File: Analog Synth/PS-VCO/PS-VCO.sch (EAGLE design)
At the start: 44 parts, among them IC1 TL084D, Q1 BC847BS, Q2 2N3906, T1 2N3904, T2 2N3904

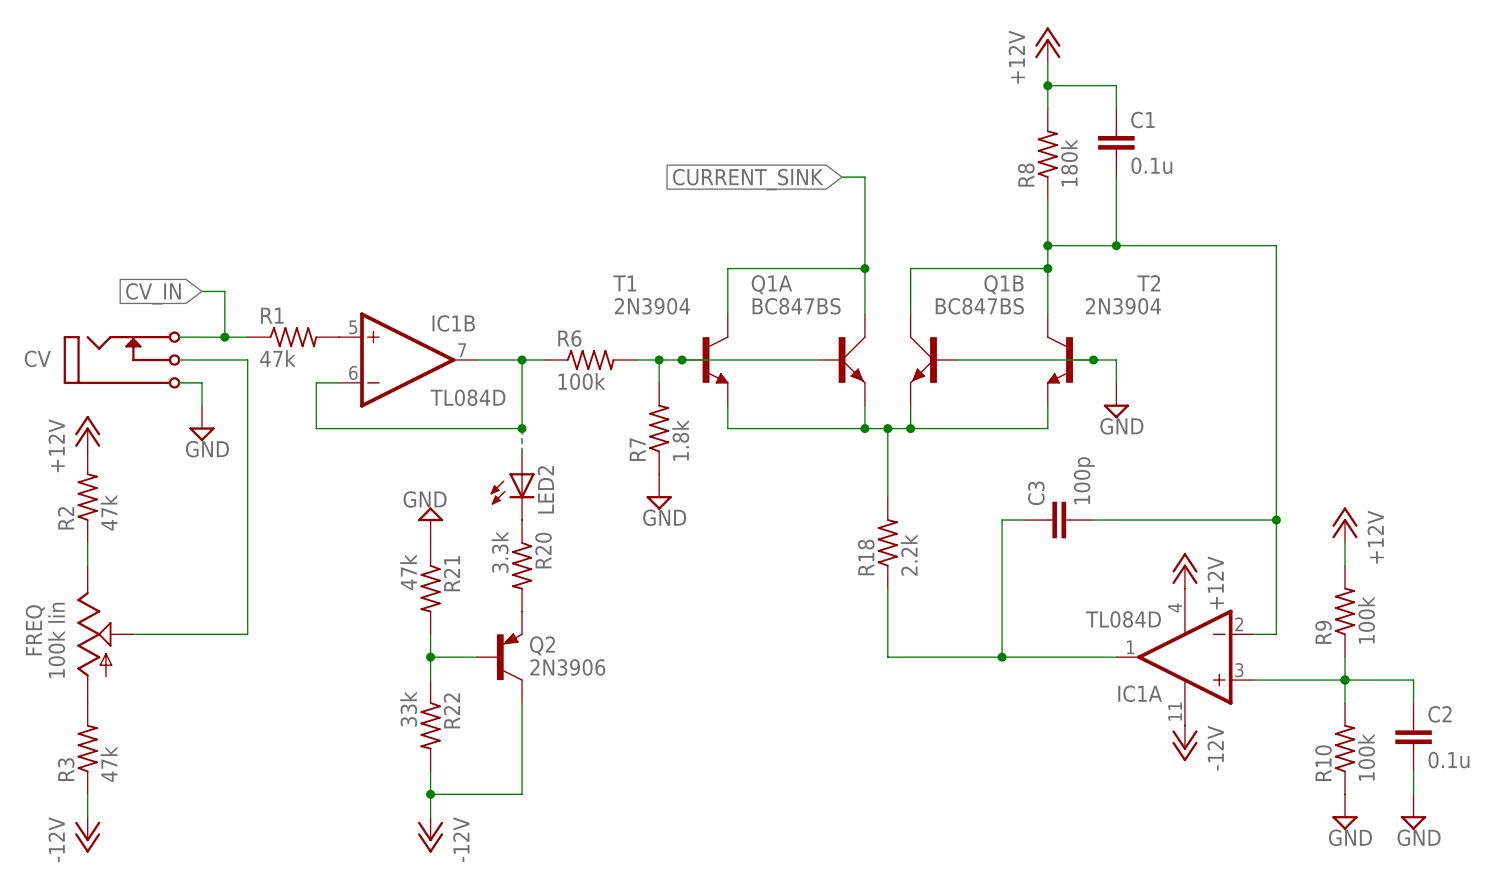
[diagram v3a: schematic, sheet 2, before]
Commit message: PS-VCO: updating documentation and schematic. rendered pdfs for schematic and pcb. generated a BOM
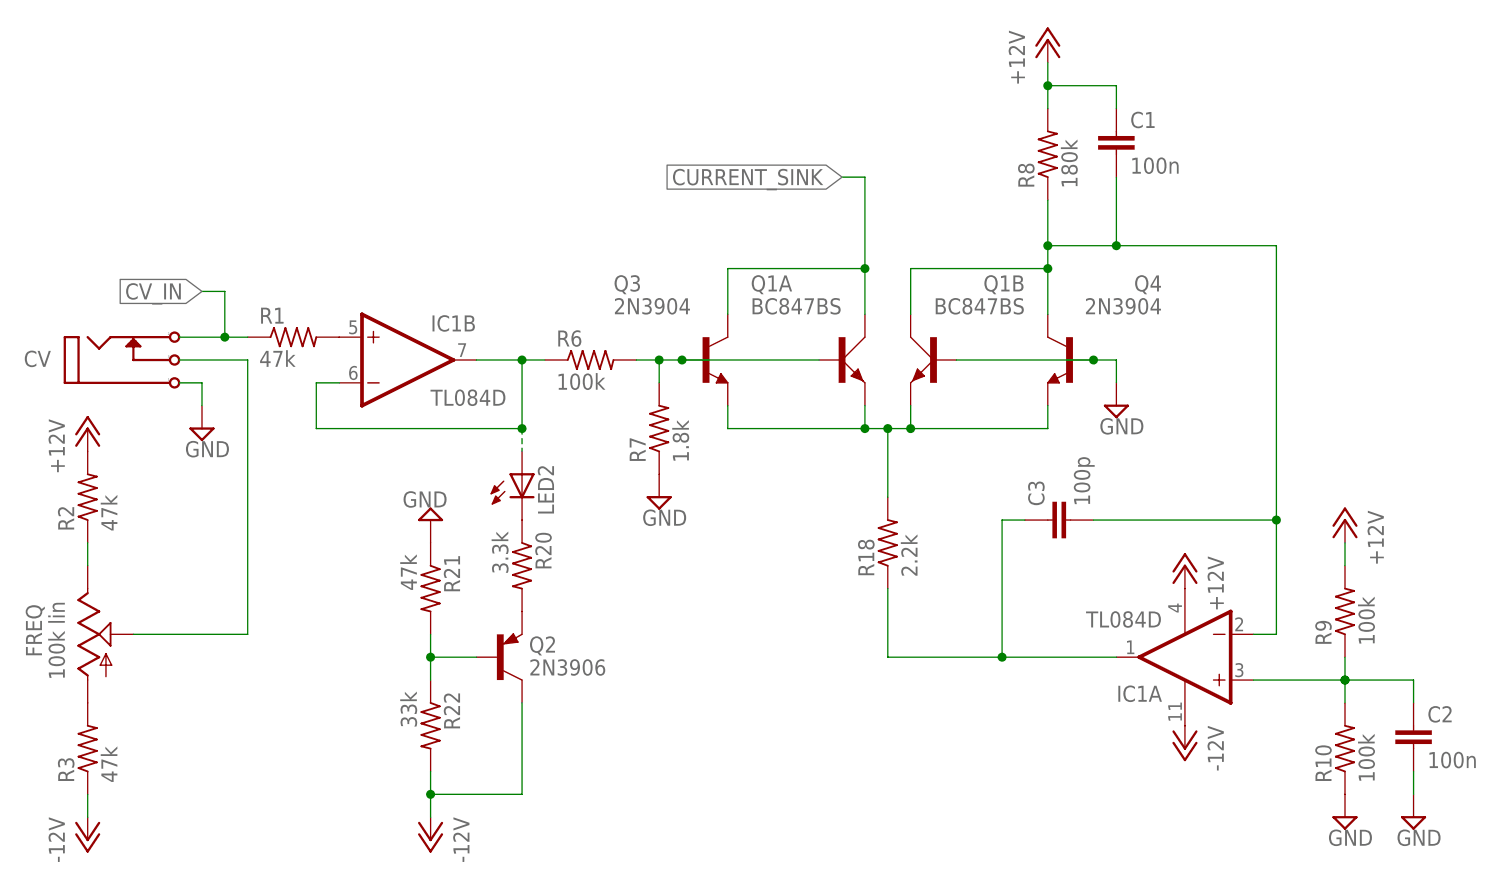
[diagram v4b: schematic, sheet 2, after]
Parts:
- C1, C2, C5: value 0.1u -> 100n
- CV: value I/O -> CV
- renumbered T1 to Q3, T2 to Q4, U$2 to Q5
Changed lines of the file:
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@@
 <parts>
 <part name="IC1" library="linear" deviceset="TL084" device="D"/>
-<part name="CV" library="!synth_sch" deviceset="MONO_JACK" device="" value="I/O"/>
+<part name="CV" library="!synth_sch" deviceset="MONO_JACK" device="" value="CV"/>
 <part name="Q1" library="transistor-small-signal" deviceset="BC847BS" device=""/>
-<part name="T1" library="transistor" deviceset="2N3904" device=""/>
-<part name="T2" library="transistor" deviceset="2N3904" device=""/>
+<part name="Q3" library="transistor" deviceset="2N3904" device=""/>
+<part name="Q4" library="transistor" deviceset="2N3904" device=""/>
 <part name="R1" library="rcl" deviceset="R-US_" device="R0603" value="47k"/>
 <part name="FREQ" library="pot" deviceset="TRIM_US-" device="B64Y" value="100k lin"/>
@@
 <part name="R7" library="rcl" deviceset="R-US_" device="R0603" value="1.8k"/>
 <part name="SUPPLY4" library="supply2" deviceset="GND" device=""/>
-<part name="C1" library="rcl" deviceset="C-EU" device="C0603" value="0.1u"/>
+<part name="C1" library="rcl" deviceset="C-EU" device="C0603" value="100n"/>
 <part name="R8" library="rcl" deviceset="R-US_" device="R0603" value="180k"/>
-<part name="C2" library="rcl" deviceset="C-EU" device="C0603" value="0.1u"/>
+<part name="C2" library="rcl" deviceset="C-EU" device="C0603" value="100n"/>
 <part name="R9" library="rcl" deviceset="R-US_" device="R0603" value="100k"/>
 <part name="R10" library="rcl" deviceset="R-US_" device="R0603" value="100k"/>
@@
 <part name="R12" library="rcl" deviceset="R-US_" device="R0603" value="4.7"/>
 <part name="JP2" library="pinhead" deviceset="PINHD-2X5" device=""/>
-<part name="U$2" library="!synth_sch" deviceset="2N7000" device=""/>
+<part name="Q5" library="!synth_sch" deviceset="2N7000" device=""/>
 <part name="SQUARE" library="!synth_sch" deviceset="MONO_JACK" device="" value="I/O"/>
 <part name="R4" library="rcl" deviceset="R-US_" device="R0603" value="27k"/>
-<part name="C5" library="rcl" deviceset="C-EU" device="C0603" value="0.1u"/>
+<part name="C5" library="rcl" deviceset="C-EU" device="C0603" value="100n"/>
 <part name="R5" library="rcl" deviceset="R-US_" device="R0603" value="100k"/>
 <part name="R13" library="rcl" deviceset="R-US_" device="R0603" value="100k"/>
@@
 <attribute name="VALUE" x="116.84" y="91.44" size="1.778" layer="96" rot="MR0"/>
 </instance>
-<instance part="T1" gate="G1" x="81.28" y="86.36"/>
-<instance part="T2" gate="G1" x="121.92" y="86.36" rot="MR0"/>
+<instance part="Q3" gate="G1" x="81.28" y="86.36"/>
+<instance part="Q4" gate="G1" x="121.92" y="86.36" rot="MR0"/>
 <instance part="R1" gate="G$1" x="35.56" y="88.9"/>
 <instance part="FREQ" gate="G$1" x="12.7" y="55.88" smashed="yes">
@@
 <pinref part="Q1" gate="A" pin="C"/>
 <wire x1="99.06" y1="91.44" x2="99.06" y2="96.52" width="0.1524" layer="91"/>
-<pinref part="T1" gate="G1" pin="C"/>
+<pinref part="Q3" gate="G1" pin="C"/>
 <wire x1="99.06" y1="96.52" x2="83.82" y2="96.52" width="0.1524" layer="91"/>
 <wire x1="83.82" y1="96.52" x2="83.82" y2="91.44" width="0.1524" layer="91"/>
@@
 <wire x1="99.06" y1="81.28" x2="99.06" y2="78.74" width="0.1524" layer="91"/>
 <wire x1="99.06" y1="78.74" x2="83.82" y2="78.74" width="0.1524" layer="91"/>
-<pinref part="T1" gate="G1" pin="E"/>
+<pinref part="Q3" gate="G1" pin="E"/>
 <wire x1="83.82" y1="78.74" x2="83.82" y2="81.28" width="0.1524" layer="91"/>
 <pinref part="Q1" gate="B" pin="E"/>
 <wire x1="104.14" y1="81.28" x2="104.14" y2="78.74" width="0.1524" layer="91"/>
 <wire x1="104.14" y1="78.74" x2="119.38" y2="78.74" width="0.1524" layer="91"/>
-<pinref part="T2" gate="G1" pin="E"/>
+<pinref part="Q4" gate="G1" pin="E"/>
 <wire x1="119.38" y1="78.74" x2="119.38" y2="81.28" width="0.1524" layer="91"/>
 <junction x="104.14" y="78.74"/>
@@
 <pinref part="Q1" gate="A" pin="B"/>
 <wire x1="93.98" y1="86.36" x2="78.74" y2="86.36" width="0.1524" layer="91"/>
-<pinref part="T1" gate="G1" pin="B"/>
+<pinref part="Q3" gate="G1" pin="B"/>
 <wire x1="76.2" y1="86.36" x2="78.74" y2="86.36" width="0.1524" layer="91"/>
 <junction x="78.74" y="86.36"/>
@@
 <pinref part="Q1" gate="B" pin="B"/>
 <wire x1="109.22" y1="86.36" x2="124.46" y2="86.36" width="0.1524" layer="91"/>
-<pinref part="T2" gate="G1" pin="B"/>
+<pinref part="Q4" gate="G1" pin="B"/>
 <wire x1="127" y1="86.36" x2="124.46" y2="86.36" width="0.1524" layer="91"/>
 <junction x="124.46" y="86.36"/>
@@
 <pinref part="Q1" gate="B" pin="C"/>
 <wire x1="104.14" y1="91.44" x2="104.14" y2="96.52" width="0.1524" layer="91"/>
-<pinref part="T2" gate="G1" pin="C"/>
+<pinref part="Q4" gate="G1" pin="C"/>
 <wire x1="104.14" y1="96.52" x2="119.38" y2="96.52" width="0.1524" layer="91"/>
 <wire x1="119.38" y1="96.52" x2="119.38" y2="91.44" width="0.1524" layer="91"/>
@@
 <instance part="IC1" gate="C" x="50.8" y="58.42"/>
 <instance part="IC1" gate="D" x="33.02" y="5.08"/>
-<instance part="U$2" gate="G$1" x="30.48" y="88.9" rot="MR0"/>
+<instance part="Q5" gate="G$1" x="30.48" y="88.9" rot="MR0"/>
 <instance part="SQUARE" gate="J1" x="88.9" y="2.54" rot="MR0"/>
 <instance part="R4" gate="G$1" x="40.64" y="76.2" rot="R90"/>
@@
 </segment>
 <segment>
-<pinref part="U$2" gate="G$1" pin="D"/>
+<pinref part="Q5" gate="G$1" pin="D"/>
 <pinref part="P+1" gate="1" pin="+12V"/>
 <wire x1="25.4" y1="91.44" x2="25.4" y2="96.52" width="0.1524" layer="91"/>
@@
 <wire x1="27.94" y1="53.34" x2="27.94" y2="55.88" width="0.1524" layer="91"/>
 <junction x="27.94" y="55.88"/>
-<pinref part="U$2" gate="G$1" pin="S"/>
+<pinref part="Q5" gate="G$1" pin="S"/>
 <wire x1="25.4" y1="86.36" x2="25.4" y2="55.88" width="0.1524" layer="91"/>
 <junction x="25.4" y="55.88"/>
@@
 <wire x1="60.96" y1="68.58" x2="60.96" y2="88.9" width="0.1524" layer="91"/>
 <wire x1="60.96" y1="88.9" x2="33.02" y2="88.9" width="0.1524" layer="91"/>
-<pinref part="U$2" gate="G$1" pin="G"/>
+<pinref part="Q5" gate="G$1" pin="G"/>
 <junction x="60.96" y="68.58"/>
 </segment>

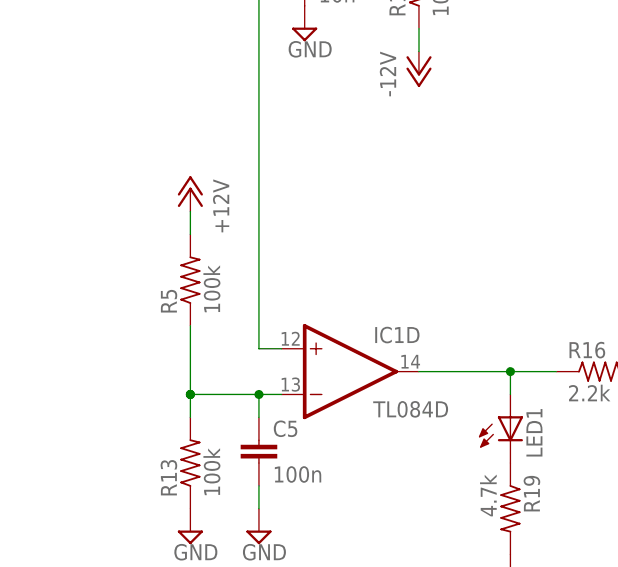
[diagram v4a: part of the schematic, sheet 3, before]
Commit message: updating PS-VCO. Changed a resistor value to get closer to 50% duty cycle. It is still very approximate, but before the duty cycle was around 25% or 30% or something really obviously not balanced.
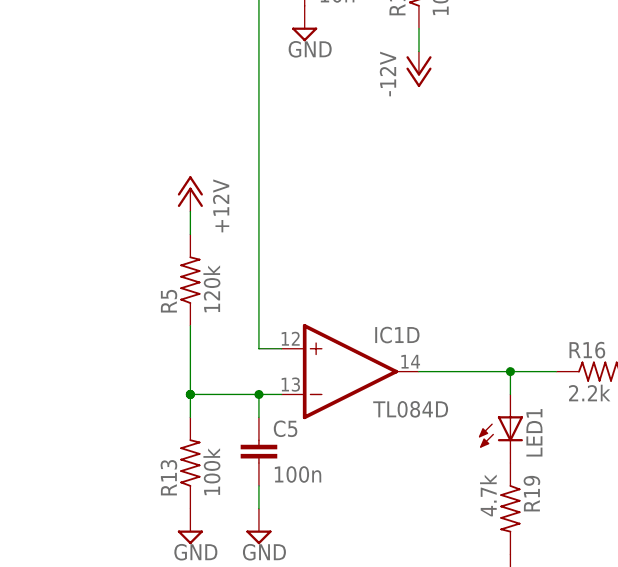
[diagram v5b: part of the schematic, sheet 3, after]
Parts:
- R5: value 100k -> 120k
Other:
- note added: "An attempt at creating a minimalistic VCO."
- note added: "This op amp (configured as a comparator) is set up to output a square wave at approximately 50% duty cycle. The amplitude of the output square wave should be just slightly less than 50% of the power rail voltage."
- note removed: "An attempt at creasing minimalistic VCO."
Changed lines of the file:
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@@
 <part name="R4" library="rcl" deviceset="R-US_" device="R0603" value="27k"/>
 <part name="C5" library="rcl" deviceset="C-EU" device="C0603" value="100n"/>
-<part name="R5" library="rcl" deviceset="R-US_" device="R0603" value="100k"/>
+<part name="R5" library="rcl" deviceset="R-US_" device="R0603" value="120k"/>
 <part name="R13" library="rcl" deviceset="R-US_" device="R0603" value="100k"/>
 <part name="C6" library="rcl" deviceset="C-EU" device="C0603" value="10n"/>
@@
 <text x="-9.144" y="100.838" size="2.54" layer="98">Ryan Jensen</text>
 <text x="-10.668" y="96.52" size="2.54" layer="98">2015-November</text>
-<text x="-36.83" y="78.74" size="2.54" layer="98">An attempt at creasing minimalistic VCO.</text>
+<text x="-36.83" y="78.74" size="2.54" layer="98">An attempt at creating a minimalistic VCO.</text>
 </plain>
 <instances>
@@
 back up to the the range and starts decreasing
 again.</text>
+<text x="-76.2" y="-2.54" size="1.778" layer="98">This op amp (configured as a comparator) is set up to
+output a square wave at approximately 50% duty cycle.
+The amplitude of the output square wave should be
+just slightly less than 50% of the power rail voltage.</text>
 </plain>
 <instances>

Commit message: adding some data to the schematic
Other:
- note added: "Experimental Data using +12 V and - 12 V supply rails output unloaded (disconnected) pot turned down to lowest frequency = 11 Hz +12 V line current draw = 8.6 mA -12 V line current draw = -8.6 mA 0 V frequency = 660 Hz +12 V line current draw = 10.1 mA -12 V line current draw = -10.0 mA pot turned up to highest frequency = 30 kHz +12 V line current draw = 14.1 mA -12 V line current draw = -13.7 mA"
- moved on the sheet: JP2
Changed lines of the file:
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@@
 <text x="-10.668" y="96.52" size="2.54" layer="98">2015-November</text>
 <text x="-36.83" y="78.74" size="2.54" layer="98">An attempt at creating a minimalistic VCO.</text>
+<text x="15.24" y="-10.16" size="1.778" layer="98">Experimental Data
+using +12 V and - 12 V supply rails
+output unloaded (disconnected)
+pot turned down to lowest frequency = 11 Hz
+  +12 V line current draw = 8.6 mA
+  -12 V line current draw = -8.6 mA
+0 V frequency = 660 Hz
+  +12 V line current draw = 10.1 mA
+  -12 V line current draw = -10.0 mA
+pot turned up to highest frequency = 30 kHz
+  +12 V line current draw = 14.1 mA
+  -12 V line current draw = -13.7 mA</text>
 </plain>
 <instances>
@@
 <instance part="R11" gate="G$1" x="-20.32" y="53.34" rot="R90"/>
 <instance part="R12" gate="G$1" x="-20.32" y="7.62" rot="R90"/>
-<instance part="JP2" gate="A" x="35.56" y="30.48"/>
+<instance part="JP2" gate="A" x="33.02" y="43.18"/>
 <instance part="C4" gate="G$1" x="-45.72" y="55.88"/>
 <instance part="C7" gate="G$1" x="-45.72" y="7.62"/>
@@
 <instance part="SUPPLY13" gate="GND" x="-40.64" y="43.18"/>
 <instance part="SUPPLY14" gate="GND" x="-40.64" y="17.78" rot="R180"/>
-<instance part="P+9" gate="1" x="25.4" y="40.64"/>
-<instance part="P-5" gate="1" x="25.4" y="25.4"/>
-<instance part="SUPPLY15" gate="GND" x="15.24" y="27.94"/>
+<instance part="P+9" gate="1" x="22.86" y="53.34"/>
+<instance part="P-5" gate="1" x="22.86" y="38.1"/>
+<instance part="SUPPLY15" gate="GND" x="12.7" y="40.64"/>
 </instances>
 <busses>
@@
 <segment>
 <pinref part="JP2" gate="A" pin="3"/>
-<wire x1="33.02" y1="33.02" x2="40.64" y2="33.02" width="0.1524" layer="91"/>
+<wire x1="30.48" y1="45.72" x2="38.1" y2="45.72" width="0.1524" layer="91"/>
 <pinref part="JP2" gate="A" pin="4"/>
-<wire x1="45.72" y1="33.02" x2="40.64" y2="33.02" width="0.1524" layer="91"/>
-<wire x1="33.02" y1="33.02" x2="15.24" y2="33.02" width="0.1524" layer="91"/>
+<wire x1="43.18" y1="45.72" x2="38.1" y2="45.72" width="0.1524" layer="91"/>
+<wire x1="30.48" y1="45.72" x2="12.7" y2="45.72" width="0.1524" layer="91"/>
 <pinref part="SUPPLY15" gate="GND" pin="GND"/>
-<wire x1="15.24" y1="33.02" x2="15.24" y2="30.48" width="0.1524" layer="91"/>
+<wire x1="12.7" y1="45.72" x2="12.7" y2="43.18" width="0.1524" layer="91"/>
 </segment>
 </net>
@@
 <pinref part="JP2" gate="A" pin="1"/>
 <pinref part="JP2" gate="A" pin="2"/>
-<wire x1="40.64" y1="35.56" x2="45.72" y2="35.56" width="0.1524" layer="91"/>
-<wire x1="40.64" y1="35.56" x2="33.02" y2="35.56" width="0.1524" layer="91"/>
-<wire x1="33.02" y1="35.56" x2="25.4" y2="35.56" width="0.1524" layer="91"/>
-<wire x1="25.4" y1="35.56" x2="25.4" y2="38.1" width="0.1524" layer="91"/>
+<wire x1="38.1" y1="48.26" x2="43.18" y2="48.26" width="0.1524" layer="91"/>
+<wire x1="38.1" y1="48.26" x2="30.48" y2="48.26" width="0.1524" layer="91"/>
+<wire x1="30.48" y1="48.26" x2="22.86" y2="48.26" width="0.1524" layer="91"/>
+<wire x1="22.86" y1="48.26" x2="22.86" y2="50.8" width="0.1524" layer="91"/>
 <pinref part="P+9" gate="1" pin="+12V"/>
 </segment>
@@
 <segment>
 <pinref part="JP2" gate="A" pin="5"/>
-<wire x1="33.02" y1="30.48" x2="40.64" y2="30.48" width="0.1524" layer="91"/>
+<wire x1="30.48" y1="43.18" x2="38.1" y2="43.18" width="0.1524" layer="91"/>
 <pinref part="JP2" gate="A" pin="6"/>
-<wire x1="45.72" y1="30.48" x2="40.64" y2="30.48" width="0.1524" layer="91"/>
-<wire x1="33.02" y1="30.48" x2="25.4" y2="30.48" width="0.1524" layer="91"/>
+<wire x1="43.18" y1="43.18" x2="38.1" y2="43.18" width="0.1524" layer="91"/>
+<wire x1="30.48" y1="43.18" x2="22.86" y2="43.18" width="0.1524" layer="91"/>
 <pinref part="P-5" gate="1" pin="-12V"/>
-<wire x1="25.4" y1="30.48" x2="25.4" y2="27.94" width="0.1524" layer="91"/>
+<wire x1="22.86" y1="43.18" x2="22.86" y2="40.64" width="0.1524" layer="91"/>
 </segment>
 </net>
@@
 <segment>
 <pinref part="JP2" gate="A" pin="7"/>
-<wire x1="33.02" y1="27.94" x2="27.94" y2="27.94" width="0.1524" layer="91"/>
-<wire x1="33.02" y1="27.94" x2="40.64" y2="27.94" width="0.1524" layer="91"/>
+<wire x1="30.48" y1="40.64" x2="25.4" y2="40.64" width="0.1524" layer="91"/>
+<wire x1="30.48" y1="40.64" x2="38.1" y2="40.64" width="0.1524" layer="91"/>
 <pinref part="JP2" gate="A" pin="8"/>
-<wire x1="53.34" y1="30.48" x2="50.8" y2="30.48" width="0.1524" layer="91"/>
-<wire x1="50.8" y1="30.48" x2="50.8" y2="27.94" width="0.1524" layer="91"/>
-<wire x1="50.8" y1="27.94" x2="40.64" y2="27.94" width="0.1524" layer="91"/>
-<label x="53.34" y="30.48" size="1.778" layer="95" xref="yes"/>
+<wire x1="50.8" y1="43.18" x2="48.26" y2="43.18" width="0.1524" layer="91"/>
+<wire x1="48.26" y1="43.18" x2="48.26" y2="40.64" width="0.1524" layer="91"/>
+<wire x1="48.26" y1="40.64" x2="38.1" y2="40.64" width="0.1524" layer="91"/>
+<label x="50.8" y="43.18" size="1.778" layer="95" xref="yes"/>
 </segment>
 </net>
@@
 <segment>
 <pinref part="JP2" gate="A" pin="9"/>
-<wire x1="33.02" y1="25.4" x2="27.94" y2="25.4" width="0.1524" layer="91"/>
-<wire x1="33.02" y1="25.4" x2="40.64" y2="25.4" width="0.1524" layer="91"/>
+<wire x1="30.48" y1="38.1" x2="25.4" y2="38.1" width="0.1524" layer="91"/>
+<wire x1="30.48" y1="38.1" x2="38.1" y2="38.1" width="0.1524" layer="91"/>
 <pinref part="JP2" gate="A" pin="10"/>
-<label x="53.34" y="25.4" size="1.778" layer="95" xref="yes"/>
-<wire x1="40.64" y1="25.4" x2="53.34" y2="25.4" width="0.1524" layer="91"/>
-</segment>
-</net>
+<label x="50.8" y="38.1" size="1.778" layer="95" xref="yes"/>
+<wire x1="38.1" y1="38.1" x2="50.8" y2="38.1" width="0.1524" layer="91"/>
+</segment>
+</net>
